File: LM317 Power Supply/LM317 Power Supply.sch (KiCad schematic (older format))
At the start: 23 parts, among them CON1 BARREL_JACK, K1 CONN_3, U1 LM317, U2 LT1206

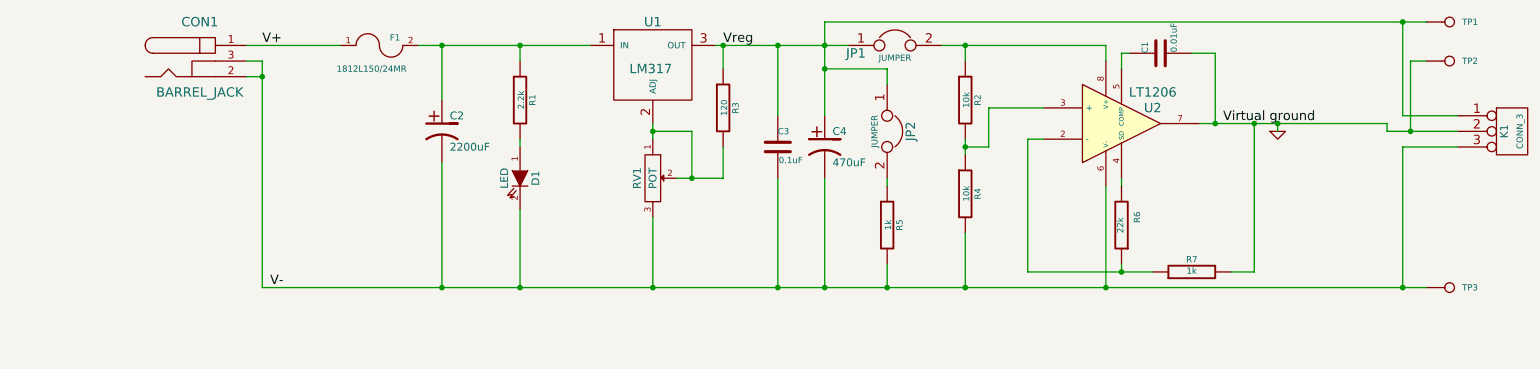
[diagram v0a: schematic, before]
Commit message: Power Supply Rev 1.3
Deleted unnecesary load, fixed potentiometer orientation and other stuff
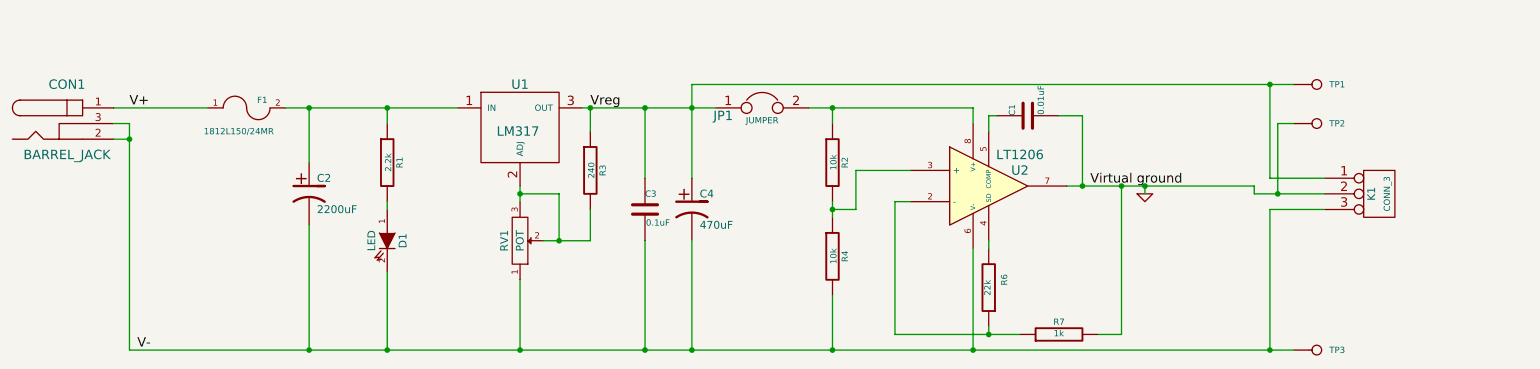
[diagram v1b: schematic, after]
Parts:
- removed JP2: JUMPER, ~, symbol JUMPER
- removed R5: 1k, ~, symbol R
- R3: value 120 -> 240
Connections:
- net V-: now also RV1.1; no longer RV1.3
- net at R3.2, RV1.2, U1.2 (ADJ): now also RV1.3; no longer RV1.1
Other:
- moved on the sheet: C1, C2, C3, C4, CON1, D1, F1, JP1, K1, R1, R2, R3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
